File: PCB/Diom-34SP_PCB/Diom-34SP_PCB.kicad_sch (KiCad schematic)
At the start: 19 parts

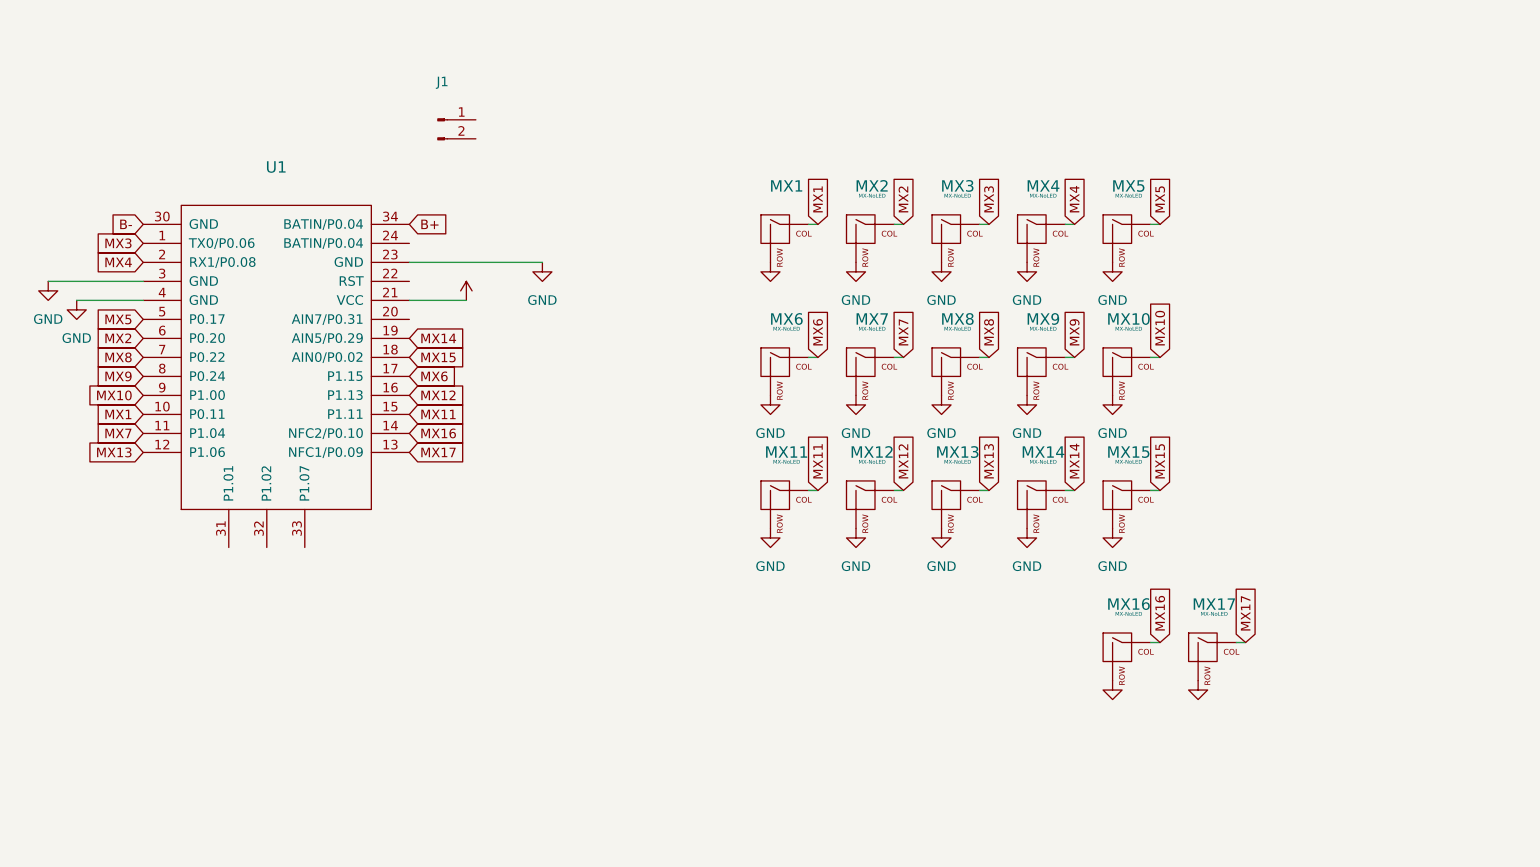
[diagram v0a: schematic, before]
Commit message: Wired Battery Connector, 1.5U Thumb Key
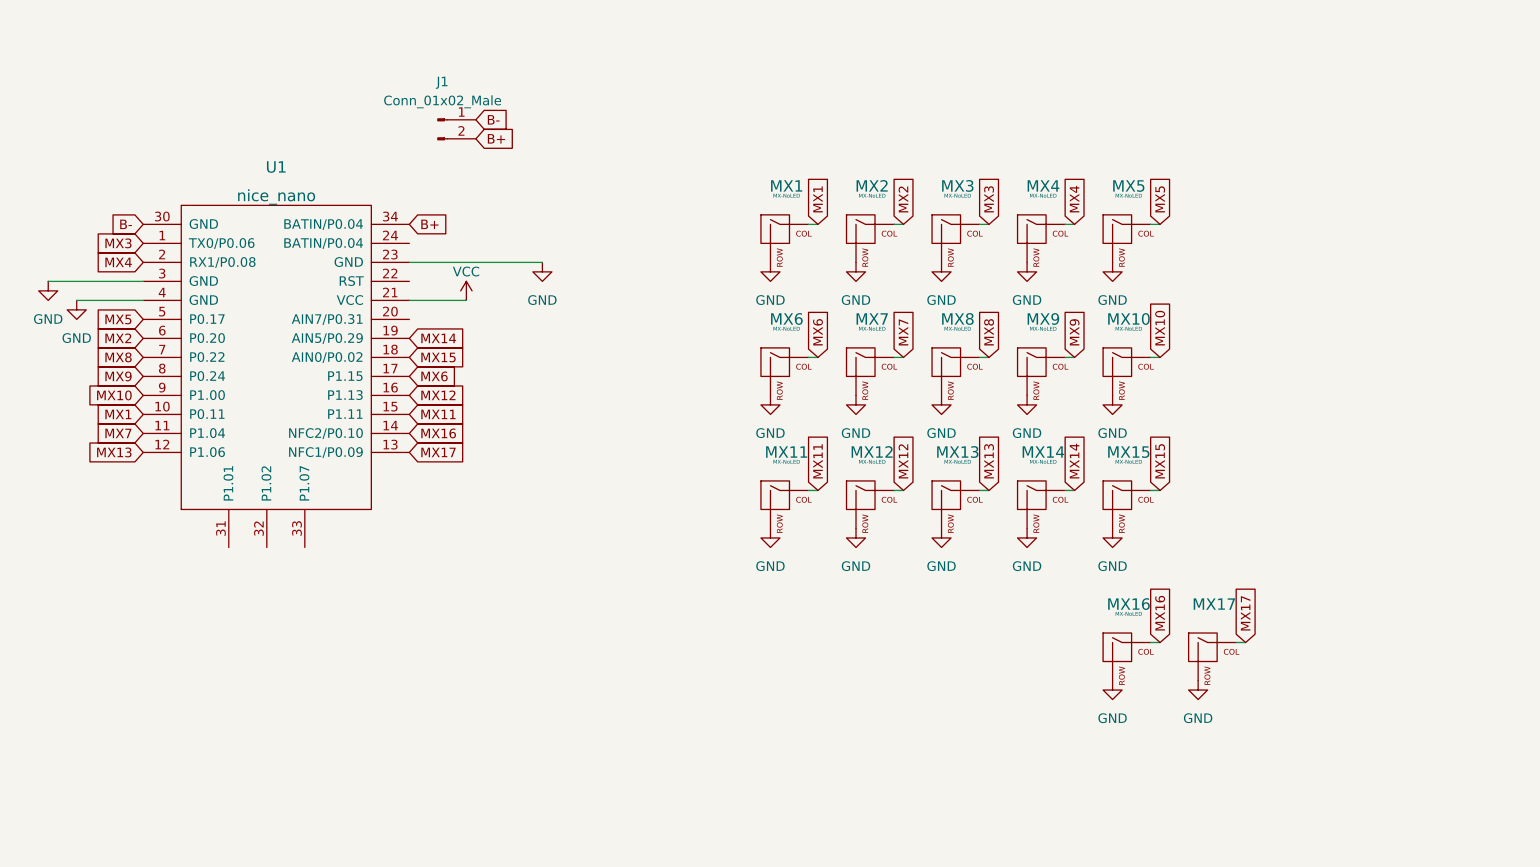
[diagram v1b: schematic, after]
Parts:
- J1: value (none) -> Conn_01x02_Male; footprint (none) -> Connector_JST:JST_EH_S2B-EH_1x02_P2.50mm_Horizontal
- MX1: value (none) -> MX-NoLED; footprint (none) -> mx-switches-doubleSided:CherryMX-1U-doubleSided
- MX10, MX11, MX12, MX13, MX14, MX15, MX16, MX2, MX3, MX4, MX5, MX6, MX7, MX8, MX9: footprint (none) -> mx-switches-doubleSided:CherryMX-1U-doubleSided
- MX17: value MX-NoLED -> (none)
- U1: value (none) -> nice_nano; footprint (none) -> nice-nano-all-pins:nice_nano
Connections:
- net B+: now also J1.2 (Pin_2)
- net B-: now also J1.1 (Pin_1)
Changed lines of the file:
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@@
+    )
+  )
+  (global_label "B-" (shape input) (at 100.33 25.4 0) (fields_autoplaced)
+    (effects (font (size 1.27 1.27)) (justify left))
+    (property "Intersheet References" "${INTERSHEET_REFS}" (id 0) (at 105.5855 25.4794 0)
+      (effects (font (size 1.27 1.27)) (justify left) hide)
     )
   )
@@
     )
   )
+  (global_label "B+" (shape input) (at 100.33 27.94 0) (fields_autoplaced)
+    (effects (font (size 1.27 1.27)) (justify left))
+    (property "Intersheet References" "${INTERSHEET_REFS}" (id 0) (at 105.5855 27.8606 0)
+      (effects (font (size 1.27 1.27)) (justify left) hide)
+    )
+  )
   (global_label "MX10" (shape input) (at 55.88 62.23 180) (fields_autoplaced)
     (effects (font (size 1.27 1.27)) (justify right))
@@
       (effects (font (size 1.27 1.27)) hide)
     )
-    (property "Value" "" (id 1) (at 99.06 45.72 0))
+    (property "Value" "VCC" (id 1) (at 99.06 45.72 0))
     (property "Footprint" "" (id 2) (at 99.06 49.53 0)
       (effects (font (size 1.27 1.27)) hide)
@@
       (effects (font (size 0.508 0.508)))
     )
-    (property "Footprint" "" (id 2) (at 159.385 41.275 0)
+    (property "Footprint" "mx-switches-doubleSided:CherryMX-1U-doubleSided" (id 2) (at 159.385 41.275 0)
       (effects (font (size 1.524 1.524)) hide)
     )
@@
       (effects (font (size 0.508 0.508)))
     )
-    (property "Footprint" "" (id 2) (at 147.955 41.275 0)
+    (property "Footprint" "mx-switches-doubleSided:CherryMX-1U-doubleSided" (id 2) (at 147.955 41.275 0)
       (effects (font (size 1.524 1.524)) hide)
     )
@@
       (effects (font (size 1.524 1.524)))
     )
-    (property "Value" "MX-NoLED" (id 1) (at 199.0056 91.44 0)
+    (property "Value" "" (id 1) (at 199.0056 91.44 0)
       (effects (font (size 0.508 0.508)))
     )
@@
       (effects (font (size 1.27 1.27)) hide)
     )
-    (property "Value" "" (id 1) (at 185.42 105.41 0))
+    (property "Value" "GND" (id 1) (at 185.42 105.41 0))
     (property "Footprint" "" (id 2) (at 185.42 100.33 0)
       (effects (font (size 1.27 1.27)) hide)
@@
       (effects (font (size 0.508 0.508)))
     )
-    (property "Footprint" "" (id 2) (at 170.815 41.275 0)
+    (property "Footprint" "mx-switches-doubleSided:CherryMX-1U-doubleSided" (id 2) (at 170.815 41.275 0)
       (effects (font (size 1.524 1.524)) hide)
     )
@@
       (effects (font (size 0.508 0.508)))
     )
-    (property "Footprint" "" (id 2) (at 147.955 76.835 0)
+    (property "Footprint" "mx-switches-doubleSided:CherryMX-1U-doubleSided" (id 2) (at 147.955 76.835 0)
       (effects (font (size 1.524 1.524)) hide)
     )
@@
       (effects (font (size 1.27 1.27)) hide)
     )
-    (property "Value" "" (id 1) (at 139.7 49.53 0))
+    (property "Value" "GND" (id 1) (at 139.7 49.53 0))
     (property "Footprint" "" (id 2) (at 139.7 44.45 0)
       (effects (font (size 1.27 1.27)) hide)
@@
       (effects (font (size 0.508 0.508)))
     )
-    (property "Footprint" "" (id 2) (at 125.095 76.835 0)
+    (property "Footprint" "mx-switches-doubleSided:CherryMX-1U-doubleSided" (id 2) (at 125.095 76.835 0)
       (effects (font (size 1.524 1.524)) hide)
     )
@@
     (in_bom yes) (on_board yes) (fields_autoplaced)
     (property "Reference" "J1" (id 0) (at 95.885 20.32 0))
-    (property "Value" "" (id 1) (at 95.885 22.86 0))
-    (property "Footprint" "" (id 2) (at 95.25 25.4 0)
+    (property "Value" "Conn_01x02_Male" (id 1) (at 95.885 22.86 0))
+    (property "Footprint" "Connector_JST:JST_EH_S2B-EH_1x02_P2.50mm_Horizontal" (id 2) (at 95.25 25.4 0)
       (effects (font (size 1.27 1.27)) hide)
     )
@@
       (effects (font (size 1.27 1.27)) hide)
     )
-    (property "Value" "" (id 1) (at 196.85 105.41 0))
+    (property "Value" "GND" (id 1) (at 196.85 105.41 0))
     (property "Footprint" "" (id 2) (at 196.85 100.33 0)
       (effects (font (size 1.27 1.27)) hide)
@@
       (effects (font (size 0.508 0.508)))
     )
-    (property "Footprint" "" (id 2) (at 170.815 97.155 0)
+    (property "Footprint" "mx-switches-doubleSided:CherryMX-1U-doubleSided" (id 2) (at 170.815 97.155 0)
       (effects (font (size 1.524 1.524)) hide)
     )
@@
       (effects (font (size 0.508 0.508)))
     )
-    (property "Footprint" "" (id 2) (at 159.385 59.055 0)
+    (property "Footprint" "mx-switches-doubleSided:CherryMX-1U-doubleSided" (id 2) (at 159.385 59.055 0)
       (effects (font (size 1.524 1.524)) hide)
     )
@@
       (effects (font (size 0.508 0.508)))
     )
-    (property "Footprint" "" (id 2) (at 147.955 59.055 0)
+    (property "Footprint" "mx-switches-doubleSided:CherryMX-1U-doubleSided" (id 2) (at 147.955 59.055 0)
       (effects (font (size 1.524 1.524)) hide)
     )
@@
       (effects (font (size 1.524 1.524)))
     )
-    (property "Value" "" (id 1) (at 73.66 35.56 0)
-      (effects (font (size 1.524 1.524)))
-    )
-    (property "Footprint" "" (id 2) (at 100.33 119.38 90)
+    (property "Value" "nice_nano" (id 1) (at 73.66 35.56 0)
+      (effects (font (size 1.524 1.524)))
+    )
+    (property "Footprint" "nice-nano-all-pins:nice_nano" (id 2) (at 100.33 119.38 90)
       (effects (font (size 1.524 1.524)) hide)
     )
@@
       (effects (font (size 0.508 0.508)))
     )
-    (property "Footprint" "" (id 2) (at 136.525 59.055 0)
+    (property "Footprint" "mx-switches-doubleSided:CherryMX-1U-doubleSided" (id 2) (at 136.525 59.055 0)
       (effects (font (size 1.524 1.524)) hide)
     )
@@
       (effects (font (size 0.508 0.508)))
     )
-    (property "Footprint" "" (id 2) (at 136.525 41.275 0)
+    (property "Footprint" "mx-switches-doubleSided:CherryMX-1U-doubleSided" (id 2) (at 136.525 41.275 0)
       (effects (font (size 1.524 1.524)) hide)
     )
@@
       (effects (font (size 0.508 0.508)))
     )
-    (property "Footprint" "" (id 2) (at 159.385 76.835 0)
+    (property "Footprint" "mx-switches-doubleSided:CherryMX-1U-doubleSided" (id 2) (at 159.385 76.835 0)
       (effects (font (size 1.524 1.524)) hide)
     )
@@
       (effects (font (size 0.508 0.508)))
     )
-    (property "Footprint" "" (id 2) (at 170.815 59.055 0)
+    (property "Footprint" "mx-switches-doubleSided:CherryMX-1U-doubleSided" (id 2) (at 170.815 59.055 0)
       (effects (font (size 1.524 1.524)) hide)
     )
@@
       (effects (font (size 0.508 0.508)))
     )
-    (property "Footprint" "" (id 2) (at 125.095 59.055 0)
+    (property "Footprint" "mx-switches-doubleSided:CherryMX-1U-doubleSided" (id 2) (at 125.095 59.055 0)
       (effects (font (size 1.524 1.524)) hide)
     )
@@
       (effects (font (size 0.508 0.508)))
     )
-    (property "Footprint" "" (id 2) (at 170.815 76.835 0)
+    (property "Footprint" "mx-switches-doubleSided:CherryMX-1U-doubleSided" (id 2) (at 170.815 76.835 0)
       (effects (font (size 1.524 1.524)) hide)
     )
@@
       (effects (font (size 0.508 0.508)))
     )
-    (property "Footprint" "" (id 2) (at 136.525 76.835 0)
+    (property "Footprint" "mx-switches-doubleSided:CherryMX-1U-doubleSided" (id 2) (at 136.525 76.835 0)
       (effects (font (size 1.524 1.524)) hide)
     )
@@
       (effects (font (size 1.524 1.524)))
     )
-    (property "Value" "" (id 1) (at 141.8556 35.56 0)
-      (effects (font (size 0.508 0.508)))
-    )
-    (property "Footprint" "" (id 2) (at 125.095 41.275 0)
+    (property "Value" "MX-NoLED" (id 1) (at 141.8556 35.56 0)
+      (effects (font (size 0.508 0.508)))
+    )
+    (property "Footprint" "mx-switches-doubleSided:CherryMX-1U-doubleSided" (id 2) (at 125.095 41.275 0)
       (effects (font (size 1.524 1.524)) hide)
     )
@@
     )
     (path "/241fc01e-7cc7-4f15-894e-dc8f64b15de6"
-      (reference "MX17") (unit 1) (value "MX-NoLED") (footprint "mx-switches-doubleSided:CherryMX-1U-doubleSided")
+      (reference "MX17") (unit 1) (value "MX-NoLED") (footprint "mx-switches-doubleSided:CherryMX-1.5U-doubleSided-Vertical")
     )
     (path "/c99fab98-5932-4f1b-aaaf-cb9175d41480"
